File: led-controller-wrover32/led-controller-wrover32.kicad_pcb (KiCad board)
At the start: 2 copper layers, 36 x 36 mm, 51 parts, among them J1 Micro_SD_Card, J2 Conn_01x12, J3 USB_B_Micro, J4 Conn_01x12, J5 Conn_01x04 DNS, J6 Conn_01x02 DNS, J7 Conn_01x03 DNS, J8 Conn_01x05, Q1 MMBT2222A-TP, Q2 MMBT2222A-TP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

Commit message: - Cleaned up the schematic - Made J5 USB D+ and D- go through protection diodes
Signed-off-by: Aaron Williams <aaron.w2@gmail.com>
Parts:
- RN1, RN4: value R_Pack02 -> 10K
- RN2: value R_Pack04 -> 10K
- U1: value XCL21X -> XCL220
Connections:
- J5 pad 2: /USB_D- -> Net-(D2-Pad3)
- J5 pad 3: /USB_D+ -> Net-(D2-Pad1)
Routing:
- net Net-(D2-Pad3): track 2.36 -> 17.2 mm
- net GND: track 66.2 -> 72.2 mm
- net Net-(D2-Pad1): track 2.20 -> 7.18 mm
- net /USB_D+: track 12.0 -> 8.46 mm
- net /USB_D-: track 10.2 -> 7.62 mm
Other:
- board text added: "Rev 1.4.4"
- board text removed: "Rev 1.4.3"
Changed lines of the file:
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@@
     (thickness 1.6)
     (drawings 84)
-    (tracks 829)
+    (tracks 838)
     (zones 0)
     (modules 51)
@@
   )
   (setup
-    (last_trace_width 0.2)
+    (last_trace_width 0.5)
     (user_trace_width 0.2)
     (user_trace_width 0.25)
@@
     (tags "resistor array")
     (attr smd)
-    (fp_text reference RN4 (at 0 1.75 180) (layer B.SilkS)
+    (fp_text reference RN4 (at -0.01 -1.96 180) (layer B.SilkS)
       (effects (font (size 1 1) (thickness 0.15)) (justify mirror))
     )
-    (fp_text value R_Pack02 (at 0 -2.1 180) (layer B.Fab)
+    (fp_text value 10K (at 0 -2.1 180) (layer B.Fab)
       (effects (font (size 1 1) (thickness 0.15)) (justify mirror))
     )
@@
       (effects (font (size 0.8 0.8) (thickness 0.1)))
     )
-    (fp_text value R_Pack02 (at 0 2.1 90) (layer F.Fab)
+    (fp_text value 10K (at 0 2.1 90) (layer F.Fab)
       (effects (font (size 1 1) (thickness 0.15)))
     )
@@
       (effects (font (size 0.8 0.8) (thickness 0.1)))
     )
-    (fp_text value R_Pack04 (at 0 2.8 90) (layer F.Fab)
+    (fp_text value 10K (at 0 2.8 90) (layer F.Fab)
       (effects (font (size 1 1) (thickness 0.15)))
     )
@@
       (net 2 GND))
     (pad 3 thru_hole oval (at 0 5.08) (size 1.7 1.7) (drill 1) (layers *.Cu *.Mask)
-      (net 58 /USB_D+))
+      (net 67 "Net-(D2-Pad1)"))
     (pad 2 thru_hole oval (at 0 2.54) (size 1.7 1.7) (drill 1) (layers *.Cu *.Mask)
-      (net 59 /USB_D-))
+      (net 68 "Net-(D2-Pad3)"))
     (pad 1 thru_hole rect (at 0 0) (size 1.7 1.7) (drill 1) (layers *.Cu *.Mask)
       (net 1 VBUS))
@@
       (effects (font (size 1 1) (thickness 0.15)))
     )
-    (fp_text value XCL21X (at -0.2 -1.1 270) (layer F.Fab)
+    (fp_text value XCL220 (at -0.2 -1.1 270) (layer F.Fab)
       (effects (font (size 1 1) (thickness 0.15)))
     )
@@
   )
   (gr_line (start 81.2 61.7) (end 82.7 62.1) (layer F.SilkS) (width 0.1))
-  (gr_text "Rev 1.4.3" (at 71.375 61.6) (layer B.SilkS)
+  (gr_text "Rev 1.4.4" (at 71.375 61.6) (layer B.SilkS)
     (effects (font (size 1.5 1.5) (thickness 0.25)) (justify mirror))
   )
@@
   (via (at 63.85 65) (size 1) (drill 0.5) (layers F.Cu B.Cu) (net 2))
   (via (at 58.85 57.1) (size 1) (drill 0.5) (layers F.Cu B.Cu) (net 2))
+  (segment (start 84.849999 71.869999) (end 84.869999 71.869999) (width 0.5) (layer B.Cu) (net 2))
+  (segment (start 84 71.02) (end 84.849999 71.869999) (width 0.5) (layer B.Cu) (net 2))
+  (segment (start 84.869999 71.869999) (end 85.15 72.15) (width 0.5) (layer B.Cu) (net 2))
+  (segment (start 83.150001 71.869999) (end 83.150001 71.899999) (width 0.5) (layer B.Cu) (net 2))
+  (segment (start 84 71.02) (end 83.150001 71.869999) (width 0.5) (layer B.Cu) (net 2))
+  (segment (start 83.150001 73.385001) (end 81.935002 74.6) (width 0.5) (layer B.Cu) (net 2))
+  (segment (start 83.150001 71.899999) (end 83.150001 73.385001) (width 0.5) (layer B.Cu) (net 2))
   (segment (start 80.45 66.75) (end 80.45 67.05) (width 0.2) (layer B.Cu) (net 3) (status 30))
   (via (at 52 65.6) (size 1) (drill 0.5) (layers F.Cu B.Cu) (net 3))
@@
   (segment (start 52.4 48.65) (end 52.4 49.472627) (width 0.2) (layer F.Cu) (net 57))
   (segment (start 52.4 49.472627) (end 54.652018 51.724645) (width 0.2) (layer F.Cu) (net 57))
-  (segment (start 81.7 64.55) (end 81.15 64.55) (width 0.2) (layer B.Cu) (net 58) (status 20))
-  (segment (start 81.79999 64.64999) (end 81.7 64.55) (width 0.2) (layer B.Cu) (net 58))
-  (segment (start 84 68.48) (end 85.150001 67.329999) (width 0.2) (layer B.Cu) (net 58) (status 10))
-  (segment (start 85.150001 65.387999) (end 84.412003 64.650001) (width 0.2) (layer B.Cu) (net 58))
-  (segment (start 85.150001 67.329999) (end 85.150001 65.387999) (width 0.2) (layer B.Cu) (net 58))
-  (segment (start 84.412003 64.650001) (end 82.273619 64.650001) (width 0.2) (layer B.Cu) (net 58))
-  (segment (start 82.273619 64.650001) (end 82.273608 64.64999) (width 0.2) (layer B.Cu) (net 58))
-  (segment (start 82.273608 64.64999) (end 81.79999 64.64999) (width 0.2) (layer B.Cu) (net 58))
-  (segment (start 82 70.7) (end 82 71.6) (width 0.2) (layer B.Cu) (net 58) (status 20))
-  (segment (start 84 68.48) (end 84 68.7) (width 0.2) (layer B.Cu) (net 58) (status 30))
-  (segment (start 84 68.7) (end 82 70.7) (width 0.2) (layer B.Cu) (net 58) (status 10))
-  (segment (start 81.775 64.55) (end 81.7 64.55) (width 0.2) (layer B.Cu) (net 58))
-  (segment (start 81.8 64.575) (end 81.775 64.55) (width 0.2) (layer B.Cu) (net 58))
-  (segment (start 83.160011 65.100011) (end 84 65.94) (width 0.2) (layer B.Cu) (net 59) (status 30))
-  (segment (start 82.087219 65.100011) (end 83.160011 65.100011) (width 0.2) (layer B.Cu) (net 59) (status 20))
-  (segment (start 82.087207 65.099999) (end 82.087219 65.100011) (width 0.2) (layer B.Cu) (net 59))
-  (segment (start 81.199999 65.099999) (end 82.087207 65.099999) (width 0.2) (layer B.Cu) (net 59) (status 10))
-  (segment (start 81.15 65.05) (end 81.199999 65.099999) (width 0.2) (layer B.Cu) (net 59) (status 30))
-  (segment (start 82.825 67.784036) (end 82.825 67.115) (width 0.2) (layer B.Cu) (net 59))
+  (segment (start 82 71.6) (end 82 70.825) (width 0.2) (layer B.Cu) (net 58))
+  (segment (start 81.7 64.55) (end 81.15 64.55) (width 0.2) (layer B.Cu) (net 58))
+  (segment (start 82.55 64.926382) (end 82.173618 64.55) (width 0.2) (layer B.Cu) (net 58))
+  (segment (start 82.173618 64.55) (end 81.7 64.55) (width 0.2) (layer B.Cu) (net 58))
+  (segment (start 82.55 70.225) (end 82.55 64.926382) (width 0.2) (layer B.Cu) (net 58))
+  (segment (start 82 70.825) (end 82 70.775) (width 0.2) (layer B.Cu) (net 58))
+  (segment (start 82 70.775) (end 82.55 70.225) (width 0.2) (layer B.Cu) (net 58))
   (segment (start 80.9125 71.6) (end 80.9125 69.696536) (width 0.2) (layer B.Cu) (net 59))
-  (segment (start 82.825 67.115) (end 84 65.94) (width 0.2) (layer B.Cu) (net 59))
-  (segment (start 80.9125 69.696536) (end 82.825 67.784036) (width 0.2) (layer B.Cu) (net 59))
+  (segment (start 81.775 65.05) (end 81.875001 65.150001) (width 0.2) (layer B.Cu) (net 59))
+  (segment (start 81.15 65.05) (end 81.775 65.05) (width 0.2) (layer B.Cu) (net 59))
+  (segment (start 80.9125 69.696536) (end 80.928464 69.696536) (width 0.2) (layer B.Cu) (net 59))
+  (segment (start 81.875001 68.749999) (end 81.875001 65.150001) (width 0.2) (layer B.Cu) (net 59))
+  (segment (start 80.928464 69.696536) (end 81.875001 68.749999) (width 0.2) (layer B.Cu) (net 59))
   (segment (start 78.424 67.85) (end 78.885 67.85) (width 0.2) (layer F.Cu) (net 62) (status 30))
   (segment (start 74.7125 59.0375) (end 75.55 58.2) (width 0.2) (layer B.Cu) (net 62))
@@
   (via (at 81.985659 72.622988) (size 0.604) (drill 0.3) (layers F.Cu B.Cu) (net 67))
   (segment (start 81.4 73.85) (end 81.4 73.122988) (width 0.2) (layer F.Cu) (net 67) (status 10))
+  (segment (start 81.985659 72.195896) (end 81.985659 72.622988) (width 0.2) (layer F.Cu) (net 67))
+  (segment (start 83.150001 70.167997) (end 81.985659 71.332339) (width 0.2) (layer F.Cu) (net 67))
+  (segment (start 81.985659 71.332339) (end 81.985659 72.195896) (width 0.2) (layer F.Cu) (net 67))
+  (segment (start 83.150001 69.329999) (end 83.150001 70.167997) (width 0.2) (layer F.Cu) (net 67))
+  (segment (start 84 68.48) (end 83.150001 69.329999) (width 0.2) (layer F.Cu) (net 67))
   (segment (start 80.75 73.85) (end 80.75 72.798628) (width 0.2) (layer F.Cu) (net 68) (status 10))
   (via (at 81.032829 72.460654) (size 0.604) (drill 0.3) (layers F.Cu B.Cu) (net 68))
@@
   (segment (start 81.032829 72.515799) (end 81.032829 72.460654) (width 0.2) (layer F.Cu) (net 68))
   (segment (start 80.777672 72.770956) (end 81.032829 72.515799) (width 0.2) (layer F.Cu) (net 68))
+  (segment (start 80.75 74.675) (end 81.1 75.025) (width 0.2) (layer F.Cu) (net 68))
+  (segment (start 80.75 73.8) (end 80.75 74.675) (width 0.2) (layer F.Cu) (net 68))
+  (segment (start 81.1 75.025) (end 84.45 75.025) (width 0.2) (layer F.Cu) (net 68))
+  (segment (start 84.45 75.025) (end 85.425 74.05) (width 0.2) (layer F.Cu) (net 68))
+  (segment (start 85.425 67.365) (end 84 65.94) (width 0.25) (layer F.Cu) (net 68))
+  (segment (start 85.425 74.05) (end 85.425 67.365) (width 0.25) (layer F.Cu) (net 68))
   (via (at 50.6 72.75) (size 0.8) (drill 0.4) (layers F.Cu B.Cu) (net 69))
   (segment (start 51.55 64) (end 51.6 64) (width 0.2) (layer F.Cu) (net 69) (status 30))

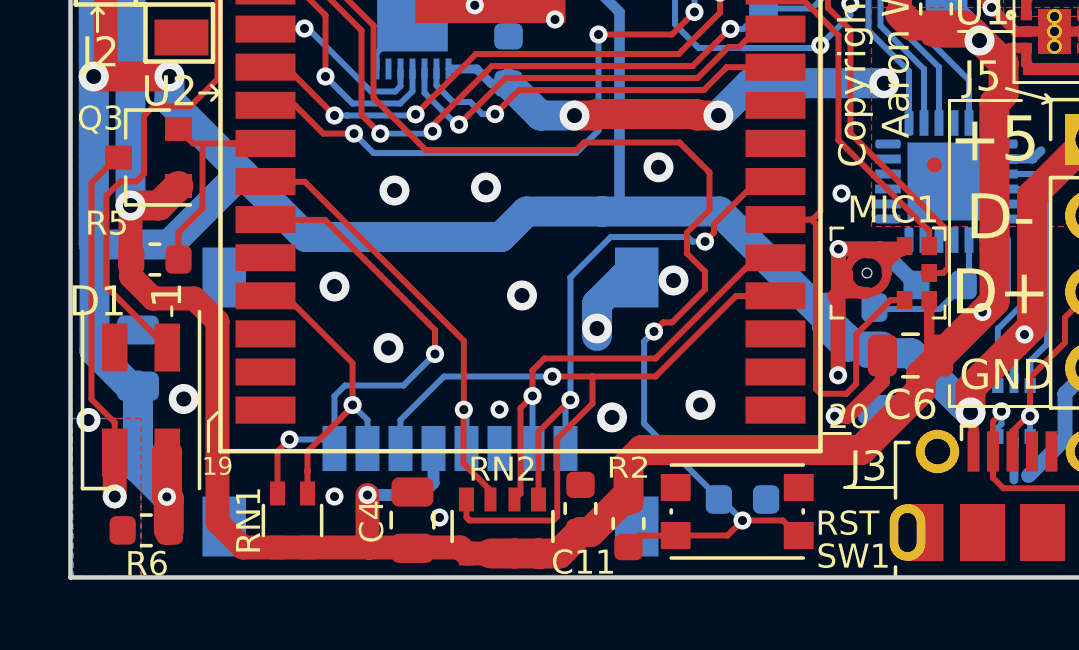
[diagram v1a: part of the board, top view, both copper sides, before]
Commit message: Fixed (hopefully) the ws1812b 3535 footprint.
Signed-off-by: Aaron Williams <aaron.w2@gmail.com>
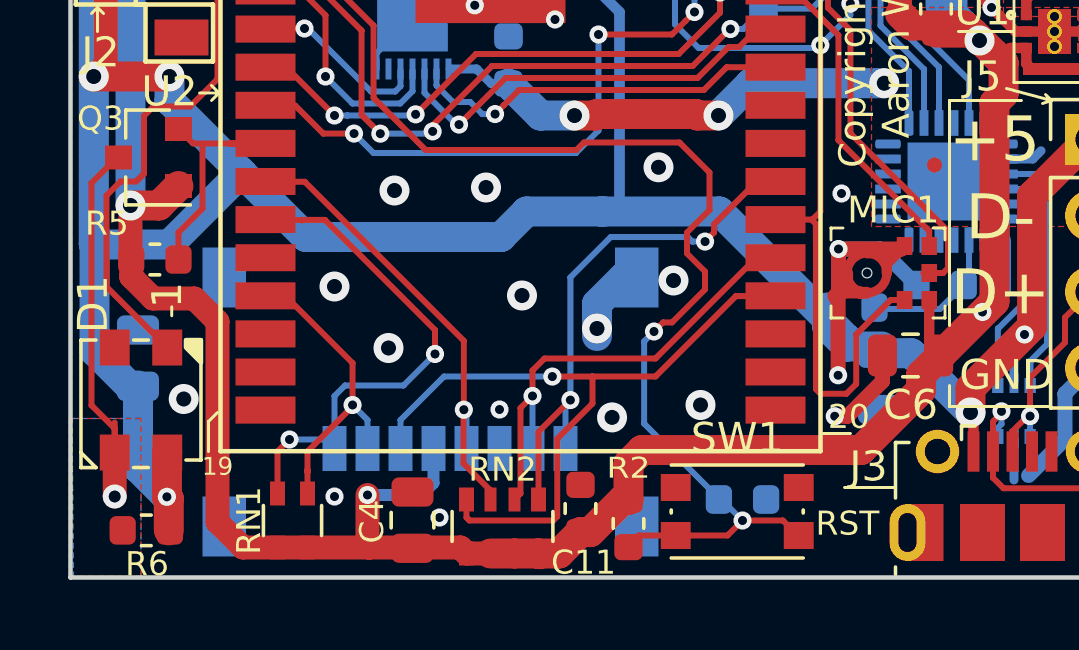
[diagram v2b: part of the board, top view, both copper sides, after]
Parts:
- D1: value SK6812MINI -> WS1812B 3535
- SW1: footprint Aaron:SW_SPST_KMR2 -> Button_Switch_SMD:SW_SPST_KMR2
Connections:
- net Net-(D2-Pad1) renamed /D+
- net Net-(D2-Pad3) renamed /D-
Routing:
- net /IO27_5V: track 12.0 -> 13.0 mm, vias 2 -> 1
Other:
- board text added: "Rev 1.4.5"
- board text removed: "Rev 1.4.4"

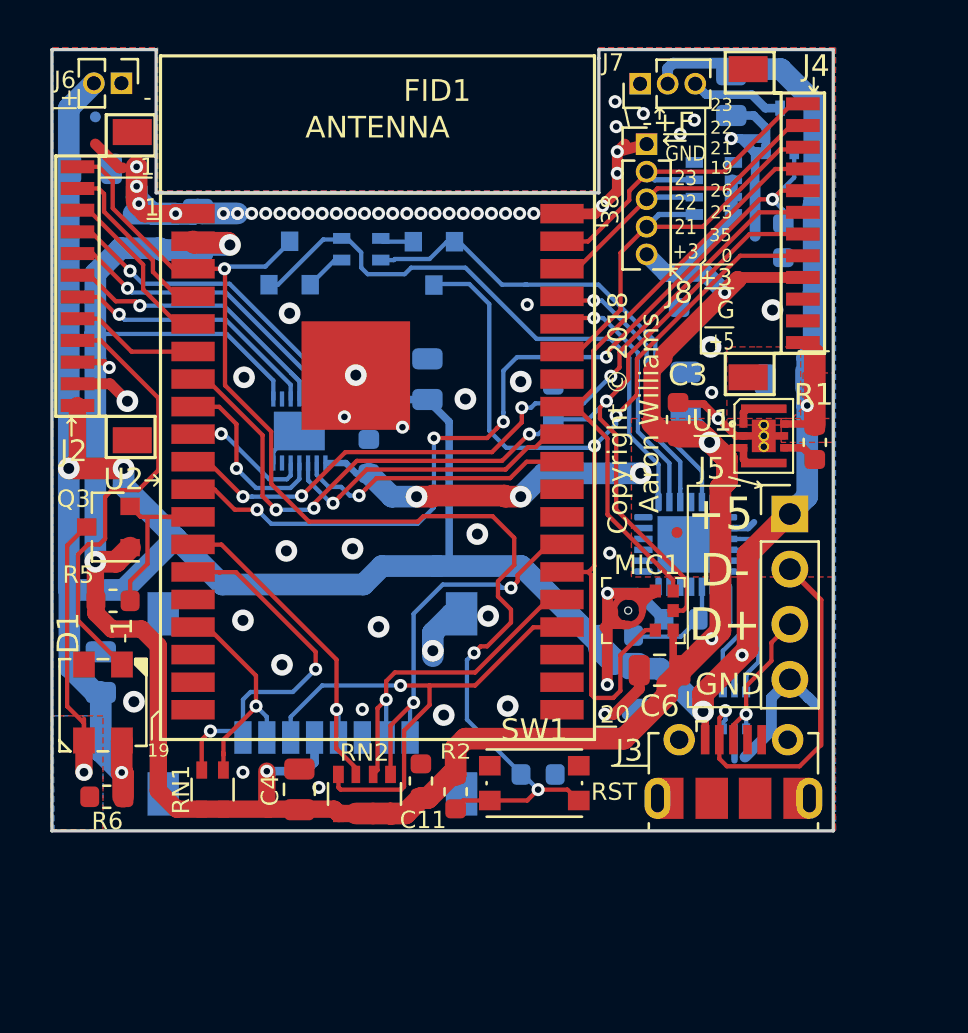
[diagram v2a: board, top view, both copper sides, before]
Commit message: This fixes a number of issues: - IO2 is now set according to the DTR and RTS signals.  This is required for   booting over the serial port. - Some more footprints were found to be using the old Kicad 4 footprints and   have been changed to KiCad 5. - One more fidicial has been added - More capacitors have been added. 	- 10uF for Wrover32 increased to 22uF 	- Some 1uF were changed to 0.1uF
Signed-off-by: Aaron Williams <aaron.w2@gmail.com>
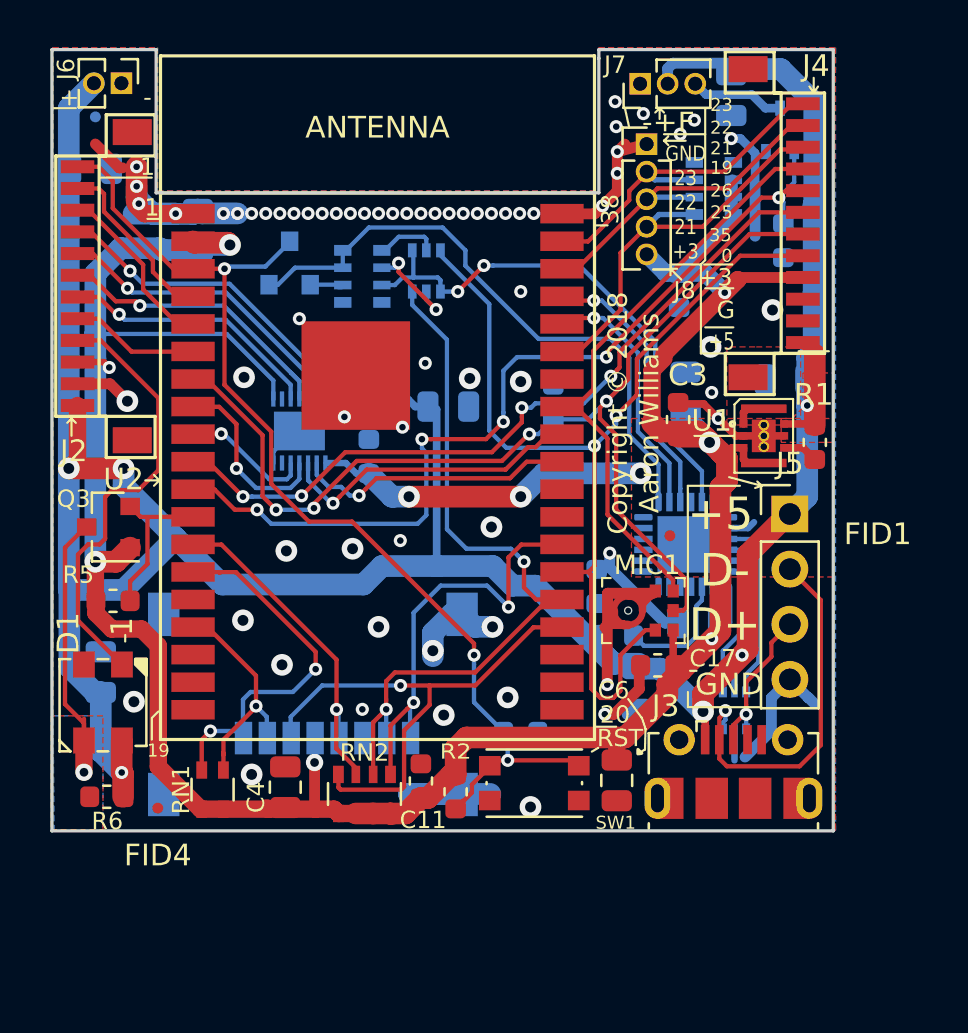
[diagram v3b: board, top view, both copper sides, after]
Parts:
- added C17: 0.1uF, Capacitor_SMD:C_0603_1608Metric, F.Cu at (77.9, 70.4)
- added C18: 10uF, Capacitor_SMD:C_0805_2012Metric, B.Cu at (79.8, 68.4)
- added FID4: FIDUCIAL_1MM, Fiducial:Fiducial_0.5mm_Dia_1mm_Outer, F.Cu at (54.9, 77.0)
- C12: value 10uF -> 22uF
- C16, C8: value 1uF -> 0.1uF
- FID1, FID2, FID3: footprint Fiducials:Fiducial_0.5mm_Dia_1mm_Outer -> Fiducial:Fiducial_0.5mm_Dia_1mm_Outer
- J1: footprint Connectors:microSD_Card_Receptacle_Wuerth_693072010801 -> Connector_Card:microSD_HC_Wuerth_693072010801
- J5: footprint Pin_Headers:Pin_Header_Straight_1x04_Pitch2.54mm -> Connector_PinHeader_2.54mm:PinHeader_1x04_P2.54mm_Vertical
- J6: footprint Pin_Headers:Pin_Header_Straight_1x02_Pitch1.27mm -> Connector_PinHeader_1.27mm:PinHeader_1x02_P1.27mm_Vertical
- J7: footprint Pin_Headers:Pin_Header_Straight_1x03_Pitch1.27mm -> Connector_PinHeader_1.27mm:PinHeader_1x03_P1.27mm_Vertical
- J8: footprint Pin_Headers:Pin_Header_Straight_1x05_Pitch1.27mm -> Connector_PinHeader_1.27mm:PinHeader_1x05_P1.27mm_Vertical
- Q1: value MMBT2222A-TP -> MMDT5551; footprint Package_TO_SOT_SMD:SOT-23 -> Package_TO_SOT_SMD:SOT-363_SC-70-6
- RN4: footprint Resistor_SMD:R_Array_Convex_2x0603 -> Resistor_SMD:R_Array_Convex_4x0603
- SW1: footprint Button_Switch_SMD:SW_SPST_KMR2 -> Aaron:SW_SPST_KMR2
- moved C6 5.45 mm to (76.0, 75.7), turned to 270 degrees
- moved R13 4.17 mm to (75.1, 66.7), turned to 90 degrees
- moved C5 2.11 mm to (71.6, 73.5)
- moved C7 1.59 mm to (68.3, 58.5), turned to 0 degrees
- moved RN4 1.25 mm to (64.3, 52.5)
- moved J1 1.18 mm to (62.0, 72.2)
- moved C4 0.66 mm to (60.8, 76.0)
- moved Q1 0.49 mm to (67.2, 52.2), turned to 90 degrees
- moved FID1 0.36 mm to (78.5, 64.4)
- turned SW1 to 180 degrees
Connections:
- Q1 pad 1: Net-(Q1-Pad1) -> /DTR
- Q1 pad 2: /DTR -> Net-(Q1-Pad2)
- Q1 pad 3: /IO0 -> /IO2
- RN4 pad 1: Net-(Q1-Pad1) -> Net-(Q1-Pad5)
- RN4 pad 2: /DTR -> Net-(Q1-Pad2)
- RN4 pad 3: Net-(Q2-Pad1) -> /DTR
- RN4 pad 4: /RTS -> Net-(RN4-Pad4)
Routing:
- net /IO2: track 16.5 -> 34.5 mm, vias 1 -> 2
- net /RESET: track 57.6 -> 50.2 mm
- net Net-(Q1-Pad2): track 0.00 -> 4.75 mm, vias 0 -> 2
- net GND: track 72.2 -> 76.8 mm
- net Net-(R12-Pad2): track 4.90 -> 8.05 mm
- net Net-(Q1-Pad5): track 0.00 -> 2.88 mm
- net /IO4: track 18.1 -> 19.9 mm
- net Net-(Q1-Pad1): track 1.54 -> 0.00 mm
- net +3V3: track 146.4 -> 144.9 mm
- net /DTR: track 23.4 -> 24.8 mm, vias 0 -> 2
- net /RTS: track 27.3 -> 28.3 mm
- net /IO14: track 16.4 -> 15.8 mm
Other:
- board text added: "Rev 1.5.0"
- board text removed: "Rev 1.4.5"
